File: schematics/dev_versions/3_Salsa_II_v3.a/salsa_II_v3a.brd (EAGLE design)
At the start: 41 x 50 mm, 55 parts, among them IC1 L293DD, IC2 74HCT04D, Q2 PMV20EN, Q3 PMV20EN, Q4 PMV20EN, Q5 PMV20EN, U1 ATMEGA168

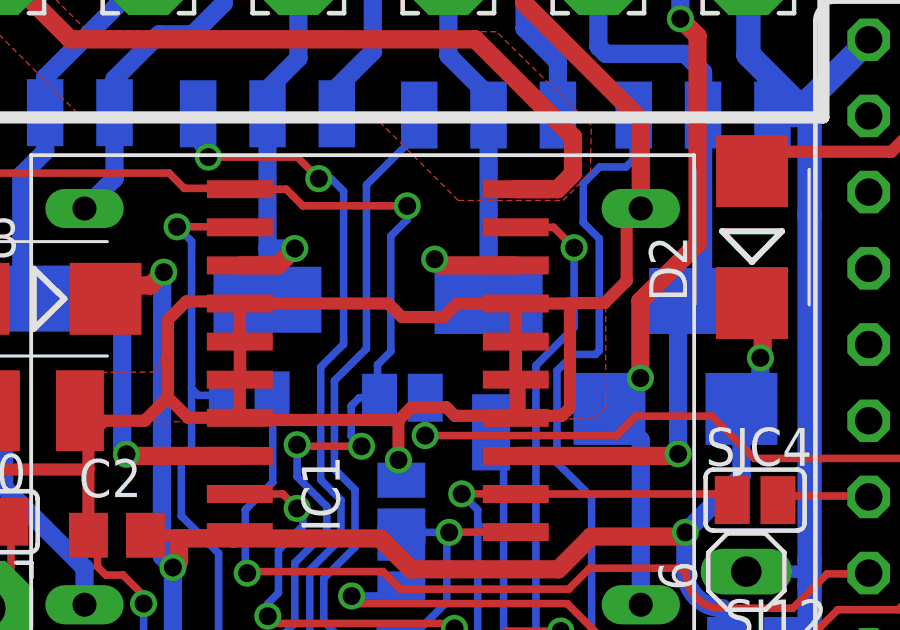
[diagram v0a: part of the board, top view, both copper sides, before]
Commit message: moved version 3 to dev as 3b was ordered
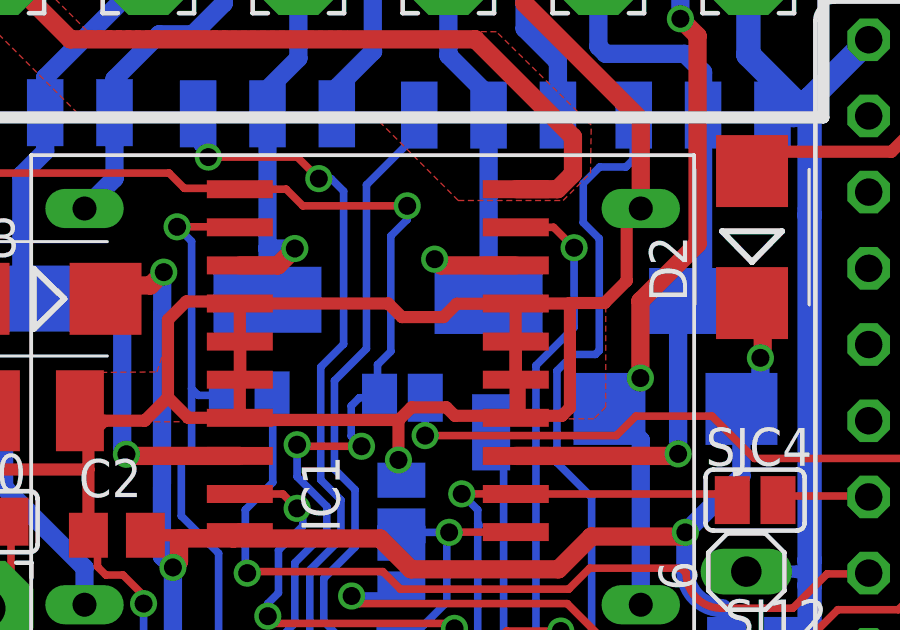
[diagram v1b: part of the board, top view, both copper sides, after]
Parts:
- Q2, Q3, Q4, Q5: value PMV20EN -> DMN6068SE-13
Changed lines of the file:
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@@
 <attribute name="VALUE" x="19.15" y="24.325" size="1.27" layer="27" rot="R180"/>
 </element>
-<element name="Q2" library="transistor-power" package="SOT223" value="PMV20EN" x="31.49" y="38.98" smashed="yes" rot="MR180">
+<element name="Q2" library="transistor-power" package="SOT223" value="DMN6068SE-13" x="31.49" y="38.98" smashed="yes" rot="MR180">
 <attribute name="NAME" x="31.7694" y="38.8657" size="1.27" layer="26" rot="MR180"/>
 </element>
-<element name="Q3" library="transistor-power" package="SOT223" value="PMV20EN" x="24.34" y="38.98" smashed="yes" rot="MR180">
+<element name="Q3" library="transistor-power" package="SOT223" value="DMN6068SE-13" x="24.34" y="38.98" smashed="yes" rot="MR180">
 <attribute name="NAME" x="24.7464" y="38.9927" size="1.27" layer="26" rot="MR180"/>
 </element>
-<element name="Q4" library="transistor-power" package="SOT223" value="PMV20EN" x="16.97" y="39.02" smashed="yes" rot="MR180">
+<element name="Q4" library="transistor-power" package="SOT223" value="DMN6068SE-13" x="16.97" y="39.02" smashed="yes" rot="MR180">
 <attribute name="NAME" x="17.7193" y="39.0708" size="1.27" layer="26" rot="MR180"/>
 </element>
-<element name="Q5" library="transistor-power" package="SOT223" value="PMV20EN" x="9.56" y="39.06" smashed="yes" rot="MR180">
+<element name="Q5" library="transistor-power" package="SOT223" value="DMN6068SE-13" x="9.56" y="39.06" smashed="yes" rot="MR180">
 <attribute name="NAME" x="6.7025" y="38.8187" size="1.27" layer="26" rot="MR180"/>
 </element>
@@
 <wire x1="31.49" y1="42.079" x2="31.49" y2="35.881" width="0.6096" layer="16"/>
 <wire x1="25.2482" y1="30.7169" x2="30.5899" y2="30.7169" width="0.6096" layer="1"/>
-<wire x1="30.81815" y1="35.20915" x2="31.49" y2="35.881" width="0.6096" layer="16"/>
+<wire x1="30.6578" y1="35.0488" x2="31.49" y2="35.881" width="0.6096" layer="16"/>
 <wire x1="30.5899" y1="30.7169" x2="30.6578" y2="30.7848" width="0.6096" layer="1"/>
 <via x="30.6578" y="30.7848" extent="1-16" drill="0.6"/>
 <wire x1="30.6578" y1="30.7848" x2="30.6578" y2="35.0488" width="0.6096" layer="16"/>
-<wire x1="30.6578" y1="35.0488" x2="30.81815" y2="35.20915" width="0.6096" layer="16"/>
 </signal>
 <signal name="PO3">
@@
 <wire x1="15.5992" y1="32.7354" x2="14.661" y2="32.7354" width="0.254" layer="16"/>
 <wire x1="14.661" y1="32.7354" x2="14.4399" y2="32.9565" width="0.254" layer="16"/>
-<wire x1="14.4399" y1="32.9565" x2="14.4399" y2="33.1597" width="0.254" layer="16"/>
-<wire x1="14.4399" y1="33.1597" x2="14.4399" y2="37.8714" width="0.254" layer="16"/>
+<wire x1="14.4399" y1="32.9565" x2="14.4399" y2="37.8714" width="0.254" layer="16"/>
 <wire x1="14.4399" y1="37.8714" x2="13.9573" y2="38.354" width="0.254" layer="16"/>
 <wire x1="15.34" y1="27.4717" x2="14.097" y2="28.7147" width="0.254" layer="16"/>
